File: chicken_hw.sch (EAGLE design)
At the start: 19 parts

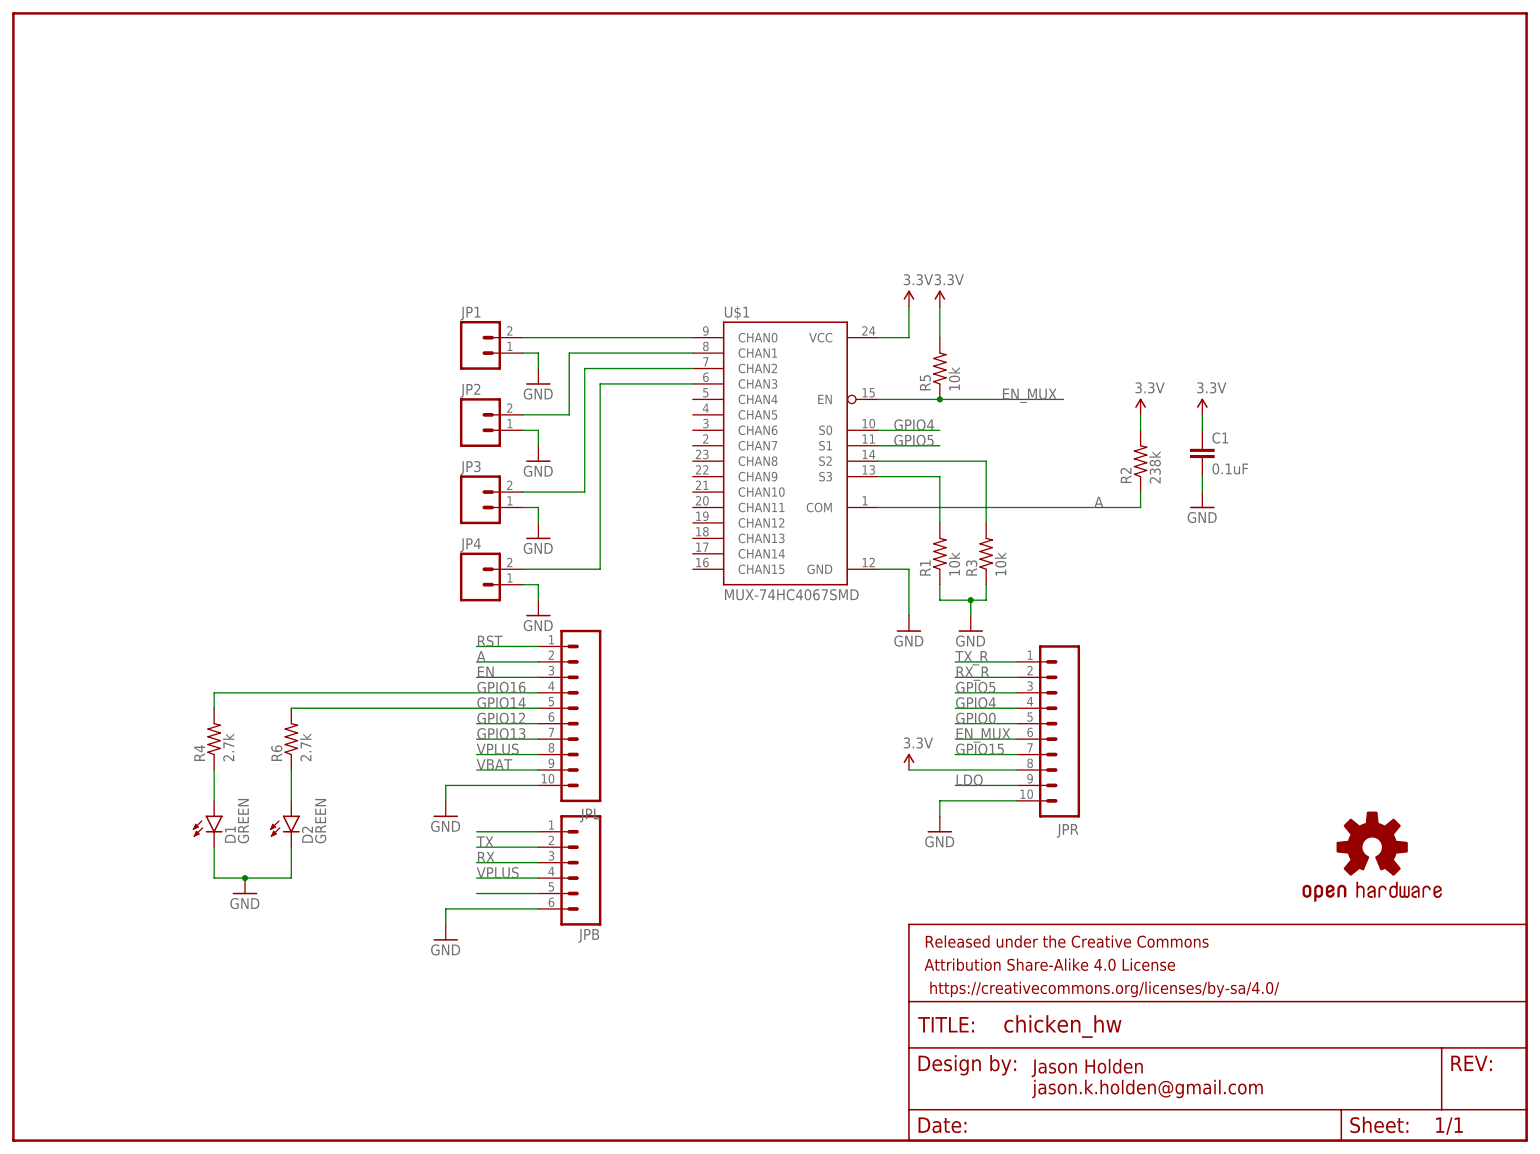
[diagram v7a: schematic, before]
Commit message: Enable ESP8266 deepsleep by connecting GPIO16 to RESET - bump to ver 0.2
Remove led's on GPIO 16,14 and move them to GPIO 12, 13
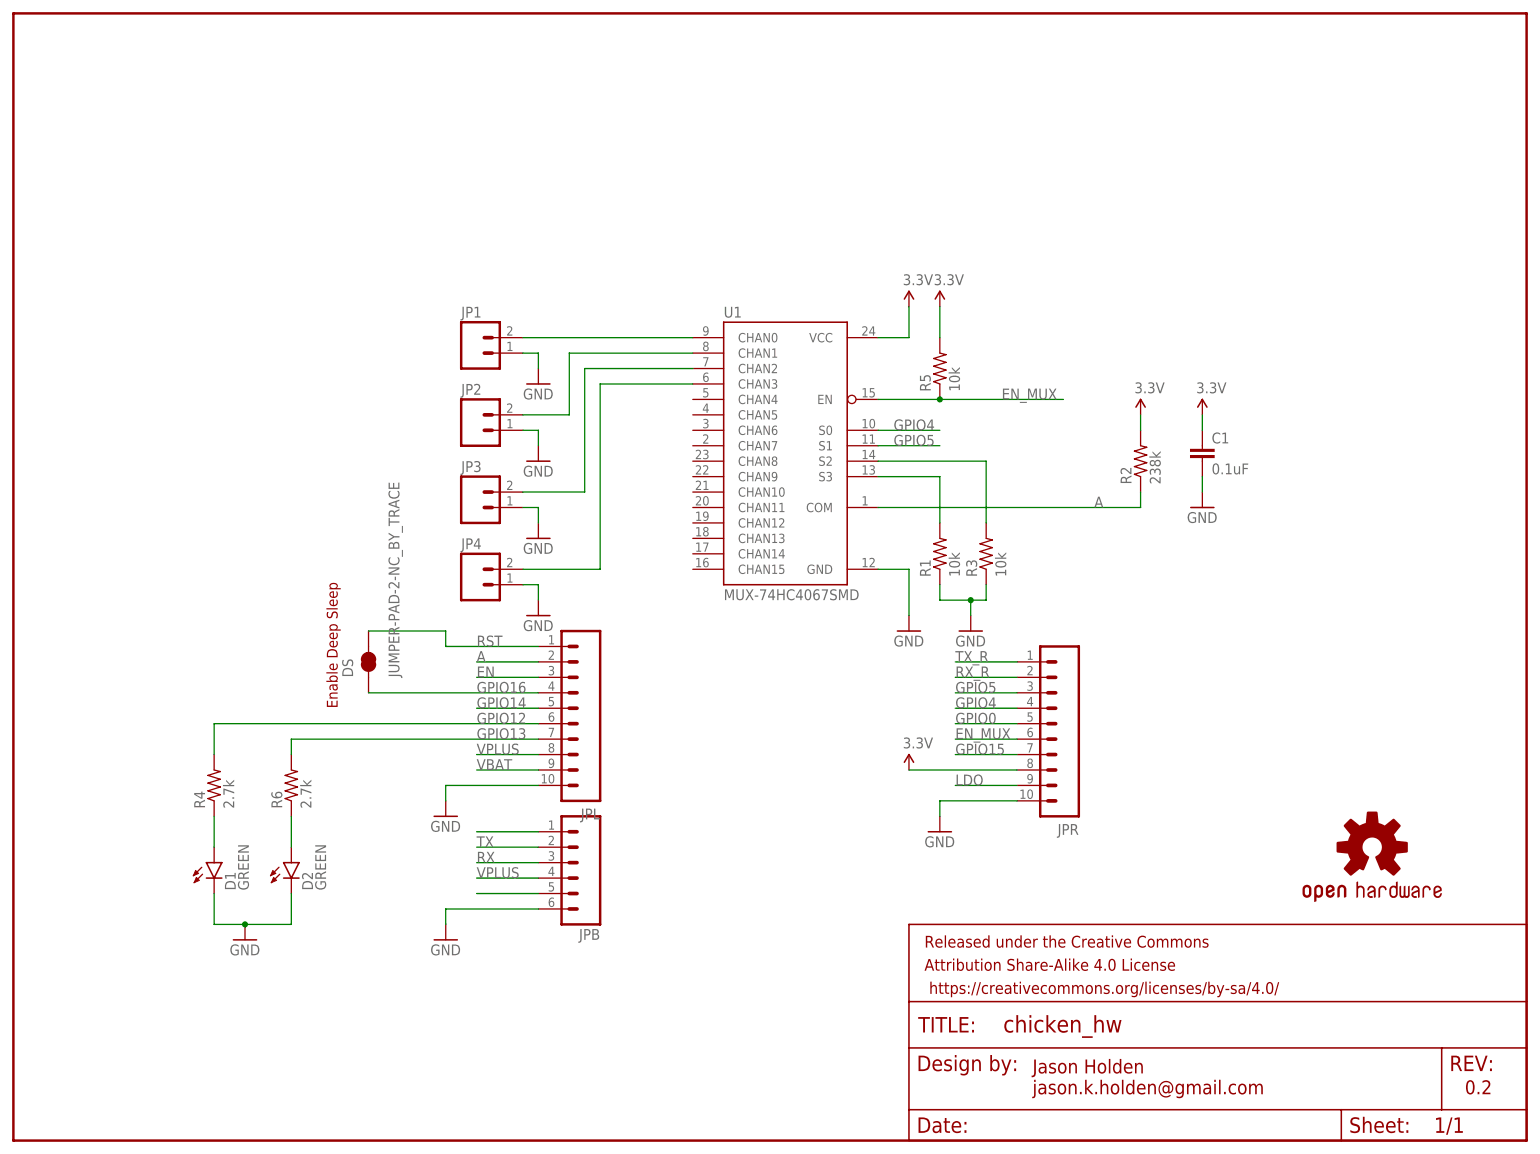
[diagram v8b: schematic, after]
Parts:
- added DS: JUMPER-PAD-2-NC_BY_TRACE, SparkFun-Passives:JUMPER-PAD-2-NC_BY_TRACE
- renumbered U$1 to U1
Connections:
- net GPIO12: now also R4.2
- net GPIO13: now also R6.2
- net GPIO14: no longer R6.2
- net GPIO16: now also DS.1; no longer R4.2
- net RST: now also DS.2
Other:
- note added: "0.2"
- note added: "Enable Deep Sleep"
- moved on the sheet: D1, D2, R4, R6
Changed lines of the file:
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@@
 <part name="GND3" library="SparkFun-Aesthetics" deviceset="GND" device=""/>
 <part name="SUPPLY1" library="SparkFun-Aesthetics" deviceset="3.3V" device=""/>
-<part name="U$1" library="SparkFun-AnalogIC" deviceset="MUX-74HC4067" device="SMD"/>
+<part name="U1" library="SparkFun-AnalogIC" deviceset="MUX-74HC4067" device="SMD"/>
 <part name="SUPPLY2" library="SparkFun-Aesthetics" deviceset="3.3V" device=""/>
 <part name="GND4" library="SparkFun-Aesthetics" deviceset="GND" device=""/>
@@
 <part name="FRAME1" library="SparkFun-Aesthetics" deviceset="FRAME-LETTER" device=""/>
 <part name="LOGO1" library="SparkFun-Aesthetics" deviceset="OSHW-LOGO" device="S"/>
+<part name="DS" library="SparkFun-Passives" deviceset="JUMPER-PAD-2-NC_BY_TRACE" device=""/>
 </parts>
 <sheets>
@@
 <text x="81.28" y="-27.94" size="2.286" layer="94" font="vector" ratio="12">Jason Holden
 jason.k.holden@gmail.com</text>
+<text x="-33.02" y="35.56" size="1.778" layer="94" rot="R90">Enable Deep Sleep</text>
+<text x="152.4" y="-27.94" size="2.286" layer="94" font="vector" ratio="12">0.2</text>
 </plain>
 <instances>
@@
 <instance part="GND3" gate="1" x="-15.24" y="17.78"/>
 <instance part="SUPPLY1" gate="G$1" x="60.96" y="25.4"/>
-<instance part="U$1" gate="G$1" x="40.64" y="78.74"/>
+<instance part="U1" gate="G$1" x="40.64" y="78.74"/>
 <instance part="SUPPLY2" gate="G$1" x="60.96" y="101.6"/>
 <instance part="GND4" gate="1" x="60.96" y="48.26"/>
@@
 <instance part="R3" gate="G$1" x="73.66" y="60.96" rot="R90"/>
 <instance part="R2" gate="G$1" x="99.06" y="76.2" rot="R90"/>
-<instance part="D1" gate="G$1" x="-53.34" y="17.78"/>
-<instance part="D2" gate="G$1" x="-40.64" y="17.78"/>
-<instance part="GND11" gate="1" x="-48.26" y="5.08"/>
-<instance part="R4" gate="G$1" x="-53.34" y="30.48" rot="R90"/>
-<instance part="R6" gate="G$1" x="-40.64" y="30.48" rot="R90"/>
+<instance part="D1" gate="G$1" x="-53.34" y="10.16"/>
+<instance part="D2" gate="G$1" x="-40.64" y="10.16"/>
+<instance part="GND11" gate="1" x="-48.26" y="-2.54"/>
+<instance part="R4" gate="G$1" x="-53.34" y="22.86" rot="R90"/>
+<instance part="R6" gate="G$1" x="-40.64" y="22.86" rot="R90"/>
 <instance part="FRAME1" gate="G$1" x="-86.36" y="-35.56"/>
 <instance part="FRAME1" gate="V" x="60.96" y="-35.56"/>
 <instance part="LOGO1" gate="G$1" x="137.16" y="12.7"/>
+<instance part="DS" gate="G$1" x="-27.94" y="43.18" rot="R90"/>
 </instances>
 <busses>
@@
 <segment>
 <pinref part="JPL" gate="G$1" pin="1"/>
-<wire x1="0" y1="45.72" x2="-10.16" y2="45.72" width="0.1524" layer="91"/>
+<wire x1="0" y1="45.72" x2="-15.24" y2="45.72" width="0.1524" layer="91"/>
 <label x="-10.16" y="45.72" size="1.778" layer="95"/>
+<wire x1="-15.24" y1="45.72" x2="-15.24" y2="48.26" width="0.1524" layer="91"/>
+<pinref part="DS" gate="G$1" pin="2"/>
+<wire x1="-15.24" y1="48.26" x2="-27.94" y2="48.26" width="0.1524" layer="91"/>
 </segment>
 </net>
@@
 </segment>
 <segment>
-<pinref part="U$1" gate="G$1" pin="COM"/>
+<pinref part="U1" gate="G$1" pin="COM"/>
 <wire x1="55.88" y1="68.58" x2="99.06" y2="68.58" width="0.1524" layer="91"/>
 <label x="91.44" y="68.58" size="1.778" layer="95"/>
@@
 </segment>
 </net>
-<net name="GPIO16" class="0">
-<segment>
-<pinref part="JPL" gate="G$1" pin="4"/>
-<label x="-10.16" y="38.1" size="1.778" layer="95"/>
-<wire x1="0" y1="38.1" x2="-53.34" y2="38.1" width="0.1524" layer="91"/>
+<net name="GPIO12" class="0">
+<segment>
+<pinref part="JPL" gate="G$1" pin="6"/>
+<label x="-10.16" y="33.02" size="1.778" layer="95"/>
+<wire x1="0" y1="33.02" x2="-53.34" y2="33.02" width="0.1524" layer="91"/>
 <pinref part="R4" gate="G$1" pin="2"/>
-<wire x1="-53.34" y1="38.1" x2="-53.34" y2="35.56" width="0.1524" layer="91"/>
-</segment>
-</net>
-<net name="GPIO14" class="0">
-<segment>
-<pinref part="JPL" gate="G$1" pin="5"/>
-<label x="-10.16" y="35.56" size="1.778" layer="95"/>
+<wire x1="-53.34" y1="33.02" x2="-53.34" y2="27.94" width="0.1524" layer="91"/>
+</segment>
+</net>
+<net name="GPIO13" class="0">
+<segment>
+<pinref part="JPL" gate="G$1" pin="7"/>
+<label x="-10.16" y="30.48" size="1.778" layer="95"/>
+<wire x1="0" y1="30.48" x2="-40.64" y2="30.48" width="0.1524" layer="91"/>
+<wire x1="-40.64" y1="30.48" x2="-40.64" y2="27.94" width="0.1524" layer="91"/>
 <pinref part="R6" gate="G$1" pin="2"/>
-<wire x1="0" y1="35.56" x2="-40.64" y2="35.56" width="0.1524" layer="91"/>
-</segment>
-</net>
-<net name="GPIO12" class="0">
-<segment>
-<pinref part="JPL" gate="G$1" pin="6"/>
-<wire x1="0" y1="33.02" x2="-10.16" y2="33.02" width="0.1524" layer="91"/>
-<label x="-10.16" y="33.02" size="1.778" layer="95"/>
-</segment>
-</net>
-<net name="GPIO13" class="0">
-<segment>
-<pinref part="JPL" gate="G$1" pin="7"/>
-<wire x1="0" y1="30.48" x2="-10.16" y2="30.48" width="0.1524" layer="91"/>
-<label x="-10.16" y="30.48" size="1.778" layer="95"/>
 </segment>
 </net>
@@
 </segment>
 <segment>
-<pinref part="U$1" gate="G$1" pin="S0"/>
+<pinref part="U1" gate="G$1" pin="S0"/>
 <wire x1="55.88" y1="81.28" x2="66.04" y2="81.28" width="0.1524" layer="91"/>
 <label x="58.42" y="81.28" size="1.778" layer="95"/>
@@
 </segment>
 <segment>
-<pinref part="U$1" gate="G$1" pin="S1"/>
+<pinref part="U1" gate="G$1" pin="S1"/>
 <wire x1="55.88" y1="78.74" x2="66.04" y2="78.74" width="0.1524" layer="91"/>
 <label x="58.42" y="78.74" size="1.778" layer="95"/>
@@
 </segment>
 <segment>
-<pinref part="U$1" gate="G$1" pin="GND"/>
+<pinref part="U1" gate="G$1" pin="GND"/>
 <wire x1="55.88" y1="58.42" x2="60.96" y2="58.42" width="0.1524" layer="91"/>
 <pinref part="GND4" gate="1" pin="GND"/>
@@
 <segment>
 <pinref part="D1" gate="G$1" pin="C"/>
-<wire x1="-53.34" y1="12.7" x2="-53.34" y2="7.62" width="0.1524" layer="91"/>
+<wire x1="-53.34" y1="5.08" x2="-53.34" y2="0" width="0.1524" layer="91"/>
 <pinref part="GND11" gate="1" pin="GND"/>
-<wire x1="-53.34" y1="7.62" x2="-48.26" y2="7.62" width="0.1524" layer="91"/>
-<wire x1="-48.26" y1="7.62" x2="-40.64" y2="7.62" width="0.1524" layer="91"/>
-<junction x="-48.26" y="7.62"/>
+<wire x1="-53.34" y1="0" x2="-48.26" y2="0" width="0.1524" layer="91"/>
+<wire x1="-48.26" y1="0" x2="-40.64" y2="0" width="0.1524" layer="91"/>
+<junction x="-48.26" y="0"/>
 <pinref part="D2" gate="G$1" pin="C"/>
-<wire x1="-40.64" y1="7.62" x2="-40.64" y2="12.7" width="0.1524" layer="91"/>
+<wire x1="-40.64" y1="0" x2="-40.64" y2="5.08" width="0.1524" layer="91"/>
 </segment>
 </net>
@@
 </segment>
 <segment>
-<pinref part="U$1" gate="G$1" pin="VCC"/>
+<pinref part="U1" gate="G$1" pin="VCC"/>
 <wire x1="55.88" y1="96.52" x2="60.96" y2="96.52" width="0.1524" layer="91"/>
 <pinref part="SUPPLY2" gate="G$1" pin="3.3V"/>
@@
 <net name="EN_MUX" class="0">
 <segment>
-<pinref part="U$1" gate="G$1" pin="EN"/>
+<pinref part="U1" gate="G$1" pin="EN"/>
 <wire x1="55.88" y1="86.36" x2="66.04" y2="86.36" width="0.1524" layer="91"/>
 <label x="76.2" y="86.36" size="1.778" layer="95"/>
@@
 <segment>
 <pinref part="JP1" gate="G$1" pin="2"/>
-<pinref part="U$1" gate="G$1" pin="CHAN0"/>
+<pinref part="U1" gate="G$1" pin="CHAN0"/>
 <wire x1="-2.54" y1="96.52" x2="25.4" y2="96.52" width="0.1524" layer="91"/>
 </segment>
@@
 <wire x1="-2.54" y1="83.82" x2="5.08" y2="83.82" width="0.1524" layer="91"/>
 <wire x1="5.08" y1="83.82" x2="5.08" y2="93.98" width="0.1524" layer="91"/>
-<pinref part="U$1" gate="G$1" pin="CHAN1"/>
+<pinref part="U1" gate="G$1" pin="CHAN1"/>
 <wire x1="5.08" y1="93.98" x2="25.4" y2="93.98" width="0.1524" layer="91"/>
 </segment>
@@
 <wire x1="-2.54" y1="71.12" x2="7.62" y2="71.12" width="0.1524" layer="91"/>
 <wire x1="7.62" y1="71.12" x2="7.62" y2="91.44" width="0.1524" layer="91"/>
-<pinref part="U$1" gate="G$1" pin="CHAN2"/>
+<pinref part="U1" gate="G$1" pin="CHAN2"/>
 <wire x1="7.62" y1="91.44" x2="25.4" y2="91.44" width="0.1524" layer="91"/>
 </segment>
@@
 <wire x1="-2.54" y1="58.42" x2="10.16" y2="58.42" width="0.1524" layer="91"/>
 <wire x1="10.16" y1="58.42" x2="10.16" y2="88.9" width="0.1524" layer="91"/>
-<pinref part="U$1" gate="G$1" pin="CHAN3"/>
+<pinref part="U1" gate="G$1" pin="CHAN3"/>
 <wire x1="10.16" y1="88.9" x2="25.4" y2="88.9" width="0.1524" layer="91"/>
 </segment>
@@
 <net name="N$1" class="0">
 <segment>
-<pinref part="U$1" gate="G$1" pin="S3"/>
+<pinref part="U1" gate="G$1" pin="S3"/>
 <wire x1="55.88" y1="73.66" x2="66.04" y2="73.66" width="0.1524" layer="91"/>
 <wire x1="66.04" y1="73.66" x2="66.04" y2="66.04" width="0.1524" layer="91"/>
@@
 <net name="N$6" class="0">
 <segment>
-<pinref part="U$1" gate="G$1" pin="S2"/>
+<pinref part="U1" gate="G$1" pin="S2"/>
 <wire x1="55.88" y1="76.2" x2="73.66" y2="76.2" width="0.1524" layer="91"/>
 <wire x1="73.66" y1="76.2" x2="73.66" y2="66.04" width="0.1524" layer="91"/>
@@
 <pinref part="R4" gate="G$1" pin="1"/>
 <pinref part="D1" gate="G$1" pin="A"/>
-<wire x1="-53.34" y1="25.4" x2="-53.34" y2="20.32" width="0.1524" layer="91"/>
+<wire x1="-53.34" y1="17.78" x2="-53.34" y2="12.7" width="0.1524" layer="91"/>
 </segment>
 </net>
@@
 <pinref part="R6" gate="G$1" pin="1"/>
 <pinref part="D2" gate="G$1" pin="A"/>
-<wire x1="-40.64" y1="25.4" x2="-40.64" y2="20.32" width="0.1524" layer="91"/>
-</segment>
-</net>
+<wire x1="-40.64" y1="17.78" x2="-40.64" y2="12.7" width="0.1524" layer="91"/>
+</segment>
+</net>
+<net name="GPIO14" class="0">
+<segment>
+<pinref part="JPL" gate="G$1" pin="5"/>
+<wire x1="-10.16" y1="35.56" x2="0" y2="35.56" width="0.1524" layer="91"/>
+<label x="-10.16" y="35.56" size="1.778" layer="95"/>
+</segment>
+</net>
+<net name="GPIO16" class="0">
+<segment>
+<pinref part="JPL" gate="G$1" pin="4"/>
+<label x="-10.16" y="38.1" size="1.778" layer="95"/>
+<pinref part="DS" gate="G$1" pin="1"/>
+<wire x1="0" y1="38.1" x2="-27.94" y2="38.1" width="0.1524" layer="91"/>
+</segment>
+</net>
